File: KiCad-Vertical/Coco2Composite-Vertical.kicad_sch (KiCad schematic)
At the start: 19 parts, among them J1 TO_COCO2, J2 AUDIO_JACK_3.5MM_KIT, Q1 PN2907, Q2 2N2222, U1 MC1372

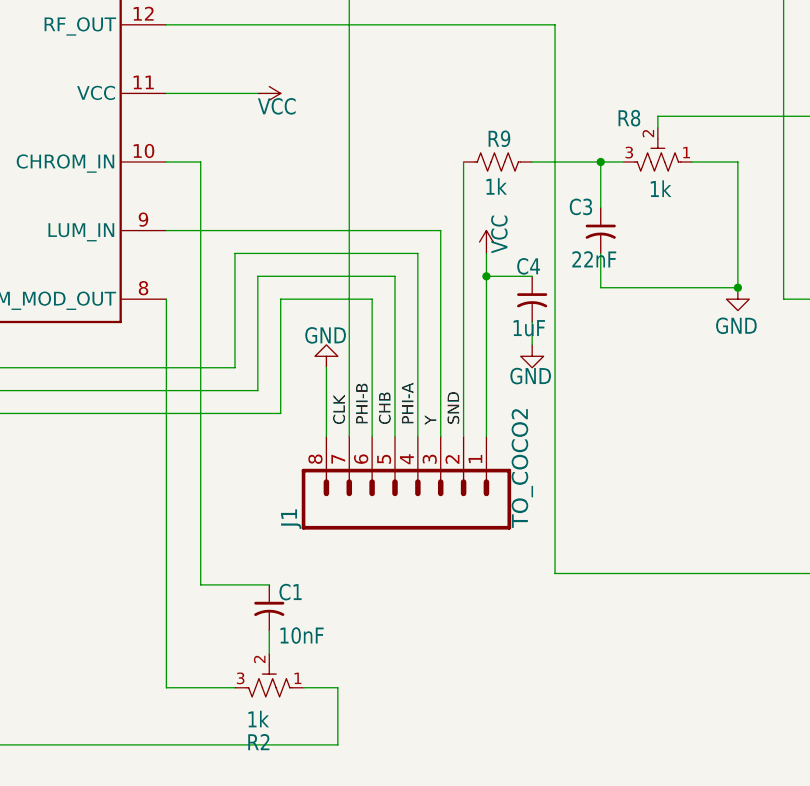
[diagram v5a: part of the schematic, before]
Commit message: Added color switch to vertical board
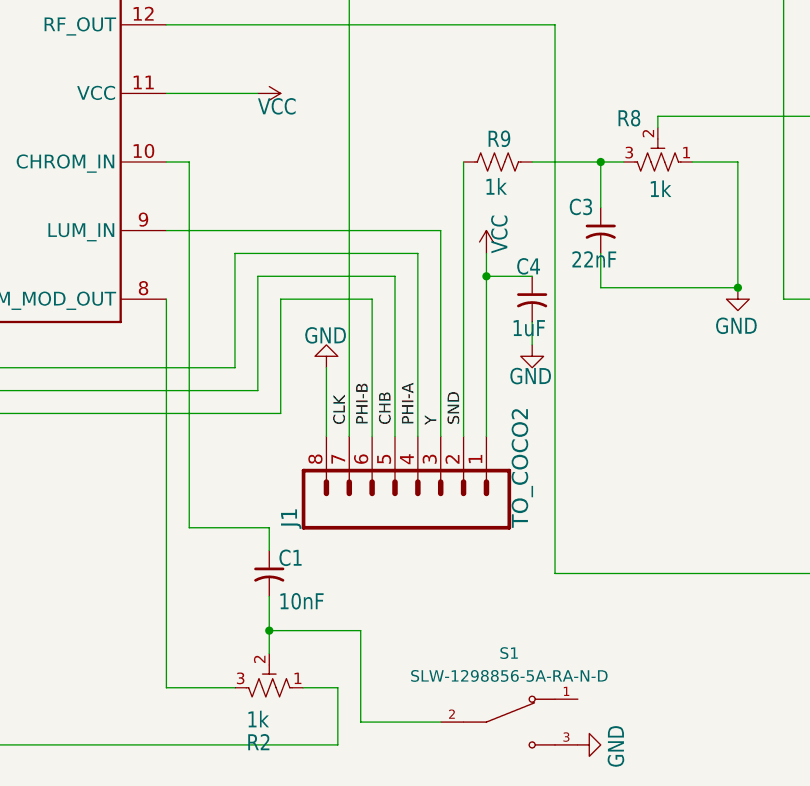
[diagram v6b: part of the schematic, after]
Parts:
- added S1: SLW-1298856-5A-RA-N-D, Imported:SW_SLW-1298856-5A-RA-N-D, symbol SLW-1298856-5A-RA-N-D:SLW-1298856-5A-RA-N-D
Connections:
- net GND: now also S1.3
- net at C1.2, R2.2: now also S1.2
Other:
- moved on the sheet: C1
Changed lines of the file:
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@@
 	(paper "A4")
 	(junction
+		(at 115.57 151.13)
+		(diameter 0)
+		(color 0 0 0 0)
+	)
+	(junction
 		(at 167.64 113.03)
 		(diameter 0)
@@
 	(wire
 		(pts
+			(xy 115.57 139.7) (xy 115.57 142.24)
+		)
+		(stroke
+			(width 0.1524)
+			(type solid)
+		)
+	)
+	(wire
+		(pts
 			(xy 223.52 109.22) (xy 223.52 96.52)
 		)
@@
 	(wire
 		(pts
+			(xy 125.73 161.29) (xy 125.73 151.13)
+		)
+		(stroke
+			(width 0)
+			(type default)
+		)
+	)
+	(wire
+		(pts
 			(xy 53.34 76.2) (xy 53.34 60.96)
 		)
@@
 	(wire
 		(pts
-			(xy 107.95 146.05) (xy 115.57 146.05)
+			(xy 106.68 139.7) (xy 115.57 139.7)
 		)
 		(stroke
@@
 	(wire
 		(pts
+			(xy 134.62 161.29) (xy 125.73 161.29)
+		)
+		(stroke
+			(width 0)
+			(type default)
+		)
+	)
+	(wire
+		(pts
 			(xy 104.14 157.48) (xy 111.76 157.48)
 		)
@@
 	(wire
 		(pts
-			(xy 104.14 99.06) (xy 107.95 99.06)
+			(xy 104.14 99.06) (xy 106.68 99.06)
 		)
 		(stroke
@@
 	(wire
 		(pts
+			(xy 125.73 151.13) (xy 115.57 151.13)
+		)
+		(stroke
+			(width 0)
+			(type default)
+		)
+	)
+	(wire
+		(pts
 			(xy 238.76 88.9) (xy 238.76 99.06)
 		)
@@
 	(wire
 		(pts
+			(xy 115.57 151.13) (xy 115.57 153.67)
+		)
+		(stroke
+			(width 0)
+			(type default)
+		)
+	)
+	(wire
+		(pts
 			(xy 48.26 127) (xy 116.84 127)
 		)
@@
 	(wire
 		(pts
-			(xy 107.95 99.06) (xy 107.95 146.05)
+			(xy 106.68 99.06) (xy 106.68 139.7)
 		)
 		(stroke
@@
 	(wire
 		(pts
-			(xy 115.57 151.13) (xy 115.57 153.67)
+			(xy 115.57 147.32) (xy 115.57 151.13)
 		)
 		(stroke
@@
 	(symbol
 		(lib_id "Device:C_Small_US")
-		(at 115.57 148.59 0)
+		(at 115.57 144.78 0)
 		(unit 1)
 		(exclude_from_sim no)
@@
 		(dnp no)
 		(property "Reference" "C1"
-			(at 116.586 147.955 0)
+			(at 116.586 144.145 0)
 			(effects
 				(font
@@
 		)
 		(property "Value" "10nF"
-			(at 116.586 152.781 0)
+			(at 116.586 148.971 0)
 			(effects
 				(font
@@
 		)
 		(property "Footprint" "Capacitor_THT:C_Disc_D3.0mm_W2.0mm_P2.50mm"
-			(at 115.57 148.59 0)
+			(at 115.57 144.78 0)
 			(effects
 				(font
@@
 		)
 		(property "Datasheet" ""
-			(at 115.57 148.59 0)
+			(at 115.57 144.78 0)
 			(effects
 				(font
@@
 		)
 		(property "Description" "capacitor, small US symbol"
-			(at 115.57 148.59 0)
+			(at 115.57 144.78 0)
 			(effects
 				(font
@@
 	)
 	(symbol
+		(lib_id "power:GND")
+		(at 149.86 163.83 90)
+		(unit 1)
+		(exclude_from_sim no)
+		(in_bom yes)
+		(on_board yes)
+		(dnp no)
+		(property "Reference" "#GND08"
+			(at 149.86 163.83 0)
+			(effects
+				(font
+					(size 1.27 1.27)
+				)
+				(hide yes)
+			)
+		)
+		(property "Value" "GND"
+			(at 155.194 166.37 0)
+			(effects
+				(font
+					(size 1.778 1.5113)
+				)
+				(justify left bottom)
+			)
+		)
+		(property "Footprint" ""
+			(at 149.86 163.83 0)
+			(effects
+				(font
+					(size 1.27 1.27)
+				)
+				(hide yes)
+			)
+		)
+		(property "Datasheet" ""
+			(at 149.86 163.83 0)
+			(effects
+				(font
+					(size 1.27 1.27)
+				)
+				(hide yes)
+			)
+		)
+		(property "Description" "Power symbol creates a global label with name \"GND\" , ground"
+			(at 149.86 163.83 0)
+			(effects
+				(font
+					(size 1.27 1.27)
+				)
+				(hide yes)
+			)
+		)
+		(pin "1"
+		)
+		(instances
+			(project "Coco2Composite-Vertical"
+				(path "/59fedd81-dfb5-41c3-969a-5c6cb0470a9a"
+					(reference "#GND08")
+					(unit 1)
+				)
+			)
+		)
+	)
+	(symbol
 		(lib_id "Device:R_US")
 		(at 185.42 114.3 90)
@@
 					(unit 1)
 				)
+			)
+		)
+	)
+	(symbol
+		(lib_id "SLW-1298856-5A-RA-N-D:SLW-1298856-5A-RA-N-D")
+		(at 142.24 161.29 0)
+		(unit 1)
+		(exclude_from_sim no)
+		(in_bom yes)
+		(on_board yes)
+		(dnp no)
+		(fields_autoplaced yes)
+		(property "Reference" "S1"
+			(at 142.24 153.67 0)
+			(effects
+				(font
+					(size 1.27 1.27)
+				)
+			)
+		)
+		(property "Value" "SLW-1298856-5A-RA-N-D"
+			(at 142.24 156.21 0)
+			(effects
+				(font
+					(size 1.27 1.27)
+				)
+			)
+		)
+		(property "Footprint" "Imported:SW_SLW-1298856-5A-RA-N-D"
+			(at 142.24 161.29 0)
+			(effects
+				(font
+					(size 1.27 1.27)
+				)
+				(justify bottom)
+				(hide yes)
+			)
+		)
+		(property "Datasheet" ""
+			(at 142.24 161.29 0)
+			(effects
+				(font
+					(size 1.27 1.27)
+				)
+				(hide yes)
+			)
+		)
+		(property "Description" ""
+			(at 142.24 161.29 0)
+			(effects
+				(font
+					(size 1.27 1.27)
+				)
+				(hide yes)
+			)
+		)
+		(property "PARTREV" "1.01"
+			(at 142.24 161.29 0)
+			(effects
+				(font
+					(size 1.27 1.27)
+				)
+				(justify bottom)
+				(hide yes)
+			)
+		)
+		(property "STANDARD" "Manufacturer Recommendations"
+			(at 142.24 161.29 0)
+			(effects
+				(font
+					(size 1.27 1.27)
+				)
+				(justify bottom)
+				(hide yes)
+			)
+		)
+		(property "MAXIMUM_PACKAGE_HEIGHT" "6.3mm"
+			(at 142.24 161.29 0)
+			(effects
+				(font
+					(size 1.27 1.27)
+				)
+				(justify bottom)
+				(hide yes)
+			)
+		)
+		(property "MANUFACTURER" "Same Sky"
+			(at 142.24 161.29 0)
+			(effects
+				(font
+					(size 1.27 1.27)
+				)
+				(justify bottom)
+				(hide yes)
+			)
+		)
+		(pin "1"
+		)
+		(pin "3"
+		)
+		(pin "2"
+		)
+		(instances
+			(project ""
+				(path "/59fedd81-dfb5-41c3-969a-5c6cb0470a9a"
+					(reference "S1")
+					(unit 1)
+				)

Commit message: Fixed associations and made cap value visible for vert board
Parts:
- Q1: footprint Package_TO_SOT_THT:TO-92_Inline_Wide -> Package_TO_SOT_THT:TO-92
- R2, R3, R8: footprint Potentiometer_THT:Potentiometer_Bourns_3296W_Vertical -> Modified:Potentiometer_Bourns_3266Y_Vertical
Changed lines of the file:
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@@
 			)
 		)
-		(property "Footprint" "Potentiometer_THT:Potentiometer_Bourns_3296W_Vertical"
+		(property "Footprint" "Modified:Potentiometer_Bourns_3266Y_Vertical"
 			(at 158.75 99.06 0)
 			(effects
@@
 			)
 		)
-		(property "Footprint" "Potentiometer_THT:Potentiometer_Bourns_3296W_Vertical"
+		(property "Footprint" "Modified:Potentiometer_Bourns_3266Y_Vertical"
 			(at 115.57 157.48 0)
 			(effects
@@
 			)
 		)
-		(property "Footprint" "Potentiometer_THT:Potentiometer_Bourns_3296W_Vertical"
+		(property "Footprint" "Modified:Potentiometer_Bourns_3266Y_Vertical"
 			(at 259.08 96.52 0)
 			(effects
@@
 			)
 		)
-		(property "Footprint" "Package_TO_SOT_THT:TO-92_Inline_Wide"
+		(property "Footprint" "Package_TO_SOT_THT:TO-92"
 			(at 241.3 104.14 0)
 			(effects

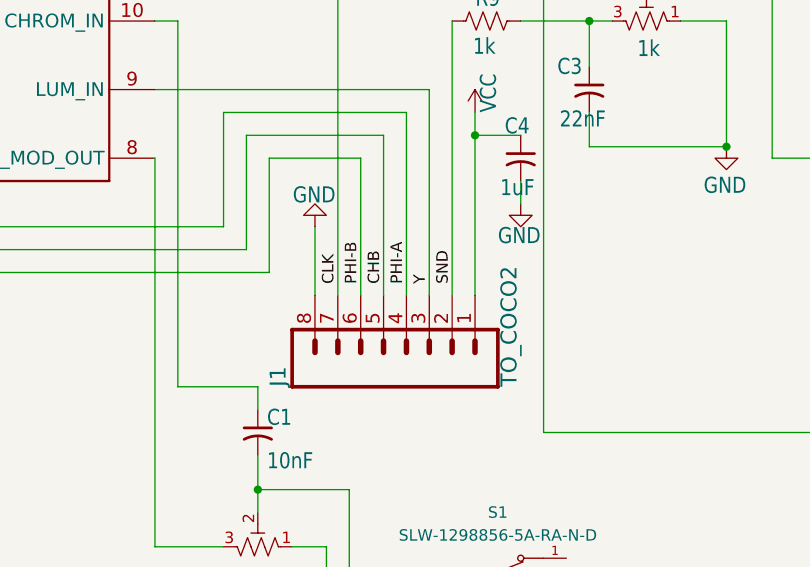
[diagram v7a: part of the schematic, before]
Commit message: Added supports for vertical board
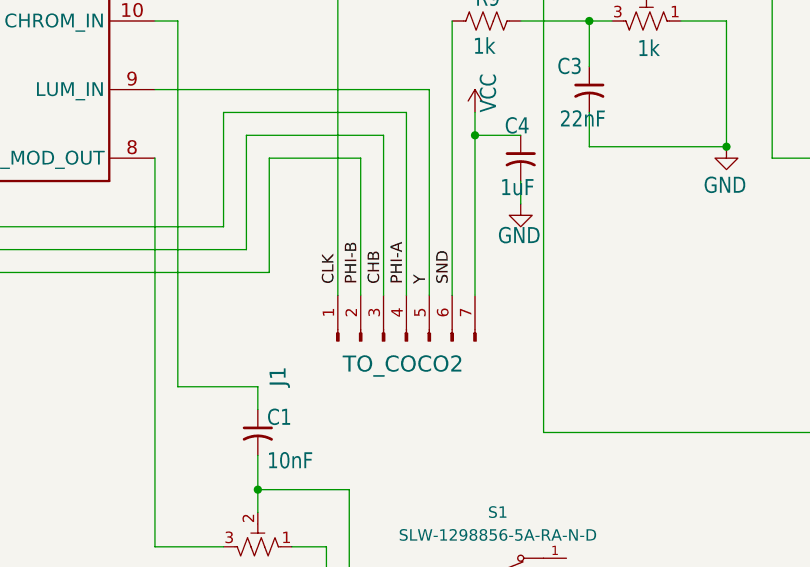
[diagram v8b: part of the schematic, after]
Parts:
- J1: footprint Connector_PinHeader_2.54mm:PinHeader_1x08_P2.54mm_Vertical -> Connector_PinHeader_2.54mm:PinHeader_1x07_P2.54mm_Vertical; symbol Coco2Composite-eagle-import:CONN_08{dblquote} -> Connector:Conn_01x07_Pin
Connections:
- net CHB: now also J1.3 (Pin_3); no longer J1.5
- net CLK: now also J1.1 (Pin_1); no longer J1.7
- net GND: no longer J1.8
- net PHI-B: now also J1.2 (Pin_2); no longer J1.6
- net SND: now also J1.6 (Pin_6); no longer J1.2
- net VCC: now also J1.7 (Pin_7); no longer J1.1
- net Y: now also J1.5 (Pin_5); no longer J1.3
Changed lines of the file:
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@@
-	(wire
-		(pts
-			(xy 121.92 129.54) (xy 121.92 121.92)
-		)
-		(stroke
-			(width 0.1524)
-			(type solid)
-		)
-	)
 	(wire
 		(pts
@@
 	)
 	(symbol
-		(lib_id "power:GND")
-		(at 121.92 121.92 180)
-		(unit 1)
-		(exclude_from_sim no)
-		(in_bom yes)
-		(on_board yes)
-		(dnp no)
-		(property "Reference" "#GND1"
-			(at 121.92 121.92 0)
-			(effects
-				(font
-					(size 1.27 1.27)
-				)
-				(hide yes)
-			)
-		)
-		(property "Value" "GND"
-			(at 124.206 117.348 0)
-			(effects
-				(font
-					(size 1.778 1.5113)
-				)
-				(justify left bottom)
-			)
-		)
-		(property "Footprint" ""
-			(at 121.92 121.92 0)
-			(effects
-				(font
-					(size 1.27 1.27)
-				)
-				(hide yes)
-			)
-		)
-		(property "Datasheet" ""
-			(at 121.92 121.92 0)
-			(effects
-				(font
-					(size 1.27 1.27)
-				)
-				(hide yes)
-			)
-		)
-		(property "Description" "Power symbol creates a global label with name \"GND\" , ground"
-			(at 121.92 121.92 0)
-			(effects
-				(font
-					(size 1.27 1.27)
-				)
-				(hide yes)
-			)
-		)
-		(pin "1"
-		)
-		(instances
-			(project ""
-				(path "/59fedd81-dfb5-41c3-969a-5c6cb0470a9a"
-					(reference "#GND1")
-					(unit 1)
-				)
-			)
-		)
-	)
-	(symbol
 		(lib_id "Device:R_Potentiometer_Trim_US")
 		(at 158.75 99.06 270)
@@
 	)
 	(symbol
-		(lib_id "Coco2Composite-eagle-import:CONN_08{dblquote}")
+		(lib_id "Connector:Conn_01x07_Pin")
 		(at 132.08 134.62 90)
 		(unit 1)
@@
 		)
 		(property "Value" "TO_COCO2"
-			(at 144.526 139.7 0)
+			(at 138.43 136.144 90)
 			(effects
 				(font
@@
 			)
 		)
-		(property "Footprint" "Connector_PinHeader_2.54mm:PinHeader_1x08_P2.54mm_Vertical"
+		(property "Footprint" "Connector_PinHeader_2.54mm:PinHeader_1x07_P2.54mm_Vertical"
 			(at 132.08 134.62 0)
 			(effects
@@
 			)
 		)
-		(property "Datasheet" ""
+		(property "Datasheet" "~"
 			(at 132.08 134.62 0)
 			(effects
@@
 			)
 		)
-		(property "Description" ""
+		(property "Description" "Generic connector, single row, 01x07, script generated"
 			(at 132.08 134.62 0)
 			(effects
@@
 		(pin "6"
 		)
-		(pin "8"
-		)
 		(pin "7"
